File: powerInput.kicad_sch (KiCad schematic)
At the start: 12 parts, among them IC11 LM74700QDBVRQ1, IC12 LM74700QDBVRQ1, IC13 LM74700QDBVRQ1, IC18 INA260AIPWR, IC8 INA260AIPWR, IC9 INA260AIPWR, Q4 BSZ067N06LS3_G, Q5 BSZ067N06LS3_G, Q6 BSZ067N06LS3_G

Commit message: Test commit
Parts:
- added C32, C39, C40: 22n, symbol Device:C_Small
- added C35: 47u, symbol Device:C_Small
- added C36, C38, C41, C43, C44, C46, C47: 100n, symbol Device:C_Small
- added C37, C42, C45, C48: 22u, symbol Device:C_Small
- added D1, D10, D11, D12, D13, D8, D9: SMCJ36A, DIOM8059X256N, symbol HEDGE2:SMCJ36A
- added IC19, IC20: LM5060Q1MM_NOPB, SOP50P490X110-10N, symbol HEDGE2:LM5060Q1MM_NOPB
- added Q15, Q16: BSZ067N06LS3_G, BSZ067N06LS3G, symbol HEDGE2:BSZ067N06LS3_G
- added R29, R37: 9k09, symbol Device:R_Small
- added R30, R38: 100k, symbol Device:R_Small
- added R31, R34: 200k, symbol Device:R_Small
- added R32, R35: 38k3, symbol Device:R_Small
- added R33, R36: 14k, symbol Device:R_Small
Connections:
- net +BATT_IN: now also IC18.12 (VBUS), C48.1, IC20.9 (OUT), Q15.5 (D_1), Q15.6 (D_2), Q15.7 (D_3), Q15.8 (D_4), Q15.9 (D_5)
- net +BENCH_IN: now also IC9.12 (VBUS)
- net +GSE_IN: now also IC8.12 (VBUS)
- net -BATT_IN: now also IC12.3 (EN), IC12.6 (ANODE), Q5.1 (S_1), Q5.2 (S_2), Q5.3 (S_3), C32.1, C36.1, D10.1 (K); no longer IC18.12 (VBUS)
- net -BENCH_IN: now also IC13.3 (EN), IC13.6 (ANODE), Q6.1 (S_1), Q6.2 (S_2), Q6.3 (S_3), C40.1, C41.1, D12.1 (K); no longer IC9.12 (VBUS)
- net -GSE_IN: now also IC11.3 (EN), IC11.6 (ANODE), Q4.1 (S_1), Q4.2 (S_2), Q4.3 (S_3), C38.1, C39.1, D9.1 (K); no longer IC8.12 (VBUS)
- net GND: now also IC11.2 (GND), IC12.2 (GND), IC13.2 (GND), C32.2, C35.2, C37.2, C39.2, C40.2, C42.2, C43.2, C44.2, C45.2, C46.2, C47.2, C48.2, D1.2 (A), D11.1 (K), D13.1 (K), D8.1 (K), IC19.6 (GND), IC20.6 (GND), R33.1, R36.1
- net at IC11.1 (VCAP): now also C38.2
- net +BUCK_BOOST: now reaches IC11.4 (CATHODE)
- net +BUCK_BOOST: now also IC12.4 (CATHODE), IC13.4 (CATHODE), Q4.5 (D_1), Q4.6 (D_2), Q4.7 (D_3), Q4.8 (D_4), Q4.9 (D_5), Q5.5 (D_1), Q5.6 (D_2), Q5.7 (D_3), Q5.8 (D_4), Q5.9 (D_5), Q6.5 (D_1), Q6.6 (D_2), Q6.7 (D_3), Q6.8 (D_4), Q6.9 (D_5), C35.1
- net at IC11.5 (GATE): now also Q4.4 (G)
- net at Q5.4 (G): now also IC12.5 (GATE)
- net at IC12.1 (VCAP): now also C36.2
- net at Q6.4 (G): now also IC13.5 (GATE)
- net at IC13.1 (VCAP): now also C41.2
- new net: IC19.1 (SENSE), R29.1
- new net: D8.2 (A), D9.2 (A)
- new net: D12.2 (A), D13.2 (A)
- new net: IC20.3 (OVP), R35.1, R36.2
- new net: IC20.4 (UVLO), R34.1, R35.2
- new net: C47.1, IC20.7 (TIMER)
- new net: IC19.3 (OVP), R32.1, R33.2
- new net: IC19.4 (UVLO), R31.1, R32.2
- new net: C44.1, IC19.7 (TIMER)
- new net: IC20.1 (SENSE), R37.1
- new net: D10.2 (A), D11.2 (A)
- new net +BATT: C37.1, C43.1, D1.1 (K), IC19.2 (VIN), Q16.1 (S_1), Q16.2 (S_2), Q16.3 (S_3), R29.2, R30.2, R31.2
- new net +BATT_INT: C42.1, C45.1, C46.1, IC19.9 (OUT), IC20.2 (VIN), Q15.1 (S_1), Q15.2 (S_2), Q15.3 (S_3), Q16.5 (D_1), Q16.6 (D_2), Q16.7 (D_3), Q16.8 (D_4), Q16.9 (D_5), R34.2, R37.2, R38.2
- new net BATTEN: IC20.5 (EN)
- new net BOUNCEBATT: IC19.5 (EN)
- new net GATE1: IC19.10 (GATE), Q16.4 (G)
- new net GATE2: IC20.10 (GATE), Q15.4 (G)
- new net STATUS1: IC19.8 (NPGD), R30.1
- new net STATUS2: IC20.8 (NPGD), R38.1
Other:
- moved on the sheet: C1, C8, C9, IC11, IC18, IC8, IC9, Q4

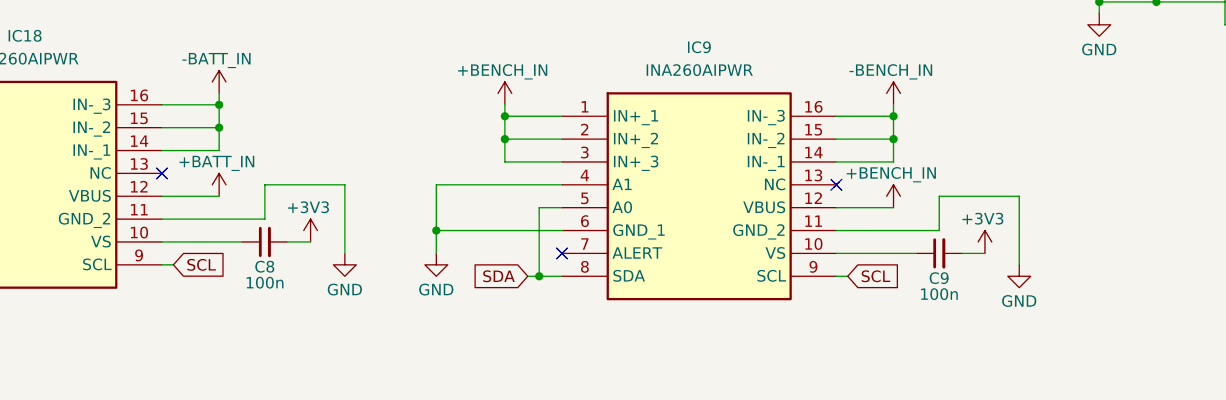
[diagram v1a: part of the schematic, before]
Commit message: Added CAN controller, got rid of one RS485 transceiver
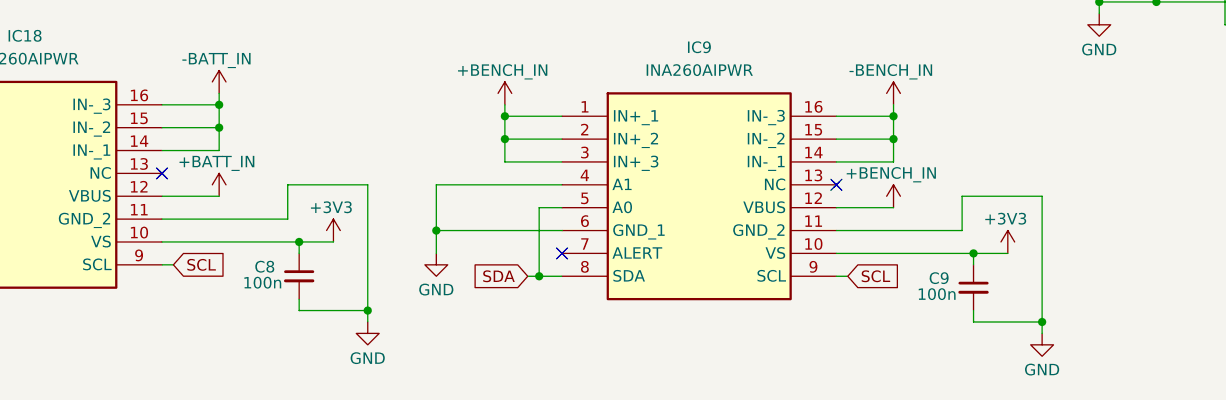
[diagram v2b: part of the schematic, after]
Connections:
- net +3V3: now also C8.1, C9.1, IC18.10 (VS), IC9.10 (VS); no longer C8.2, C9.2
- net GND: now also C8.2, C9.2

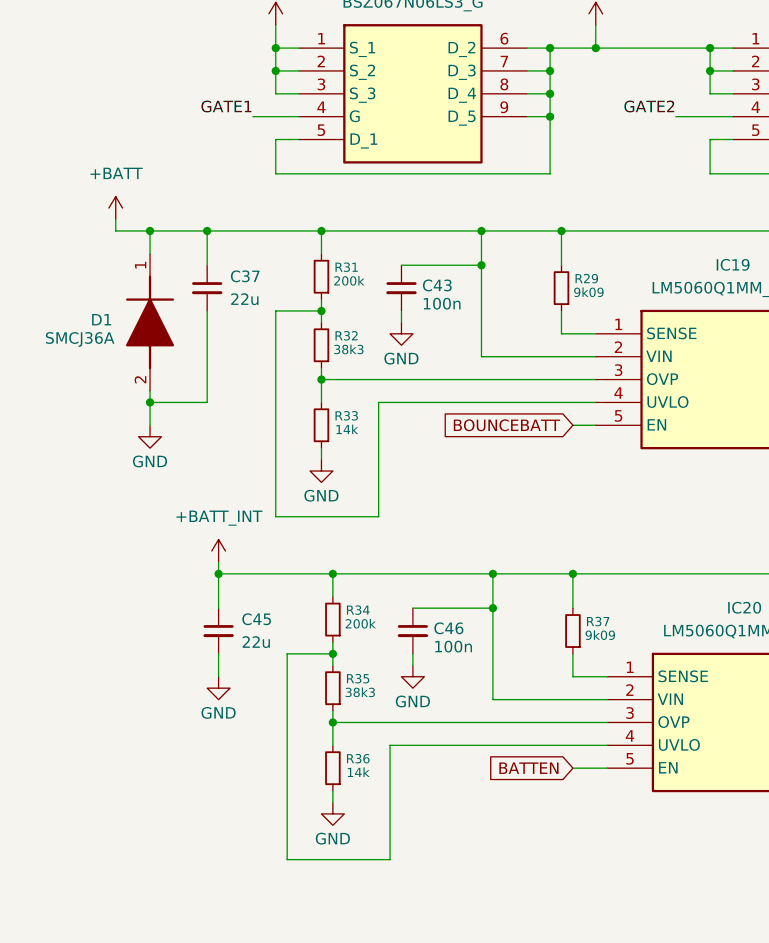
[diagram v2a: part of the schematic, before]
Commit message: updates to connectors
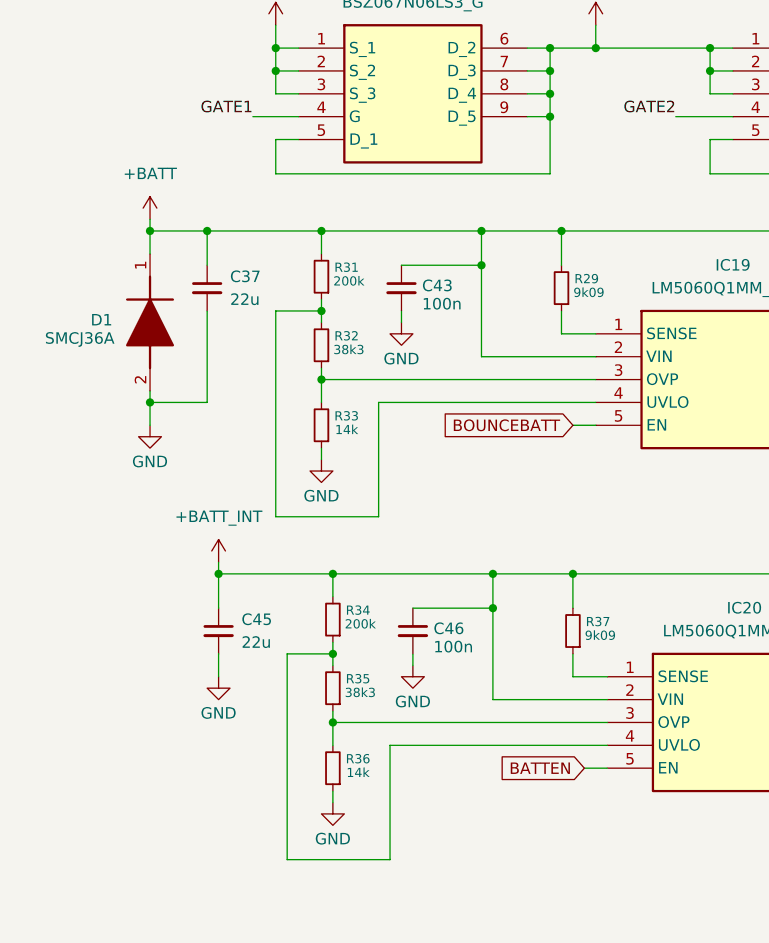
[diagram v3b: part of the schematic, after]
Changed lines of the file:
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@@
 	(title_block
 		(title "University of Virginia")
-		(date "2025-10-12")
+		(date "2025-10-30")
 		(rev "HEDGE2 EPS")
 		(company "Department of Mechanical and Aerospace Engineering")
@@
 	(wire
 		(pts
-			(xy 27.94 77.47) (xy 31.75 77.47)
-		)
-		(stroke
-			(width 0)
-			(type default)
-		)
-	)
-	(wire
-		(pts
 			(xy 228.6 113.03) (xy 259.08 113.03)
 		)
@@
 	(wire
 		(pts
-			(xy 27.94 77.47) (xy 27.94 76.2)
+			(xy 31.75 77.47) (xy 31.75 76.2)
 		)
 		(stroke
@@
 	(wire
 		(pts
+			(xy 138.43 113.03) (xy 138.43 114.3)
+		)
+		(stroke
+			(width 0)
+			(type default)
+		)
+	)
+	(wire
+		(pts
 			(xy 222.25 105.41) (xy 231.14 105.41)
 		)
@@
 	(wire
 		(pts
-			(xy 138.43 113.03) (xy 138.43 114.3)
-		)
-		(stroke
-			(width 0)
-			(type default)
-		)
-	)
-	(wire
-		(pts
 			(xy 222.25 59.69) (xy 228.6 59.69)
 		)
@@
 	(wire
 		(pts
-			(xy 78.74 137.16) (xy 82.55 137.16)
-		)
-		(stroke
-			(width 0)
-			(type default)
-		)
-	)
-	(wire
-		(pts
 			(xy 76.2 62.23) (xy 76.2 59.69)
 		)
@@
 	(wire
 		(pts
+			(xy 80.01 137.16) (xy 82.55 137.16)
+		)
+		(stroke
+			(width 0)
+			(type default)
+		)
+	)
+	(wire
+		(pts
 			(xy 182.88 130.81) (xy 228.6 130.81)
 		)
@@
 	(global_label "BATTEN"
 		(shape input)
-		(at 78.74 137.16 180)
+		(at 80.01 137.16 180)
 		(fields_autoplaced yes)
 		(effects
@@
 		)
 		(property "Intersheetrefs" "${INTERSHEET_REFS}"
-			(at 68.9815 137.16 0)
+			(at 70.2515 137.16 0)
 			(effects
 				(font
@@
 	(symbol
 		(lib_id "power:+BATT")
-		(at 27.94 76.2 0)
+		(at 31.75 76.2 0)
 		(unit 1)
 		(exclude_from_sim no)
@@
 		(fields_autoplaced yes)
 		(property "Reference" "#PWR079"
-			(at 27.94 80.01 0)
+			(at 31.75 80.01 0)
 			(effects
 				(font
@@
 		)
 		(property "Value" "+BATT"
-			(at 27.94 71.12 0)
+			(at 31.75 71.12 0)
 			(effects
 				(font
@@
 		)
 		(property "Footprint" ""
-			(at 27.94 76.2 0)
+			(at 31.75 76.2 0)
 			(effects
 				(font
@@
 		)
 		(property "Datasheet" ""
-			(at 27.94 76.2 0)
+			(at 31.75 76.2 0)
 			(effects
 				(font
@@
 		)
 		(property "Description" "Power symbol creates a global label with name \"+BATT\""
-			(at 27.94 76.2 0)
+			(at 31.75 76.2 0)
 			(effects
 				(font
